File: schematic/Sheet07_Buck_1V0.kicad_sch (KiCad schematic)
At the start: 14 parts, among them U5 TPS7H5001-SP

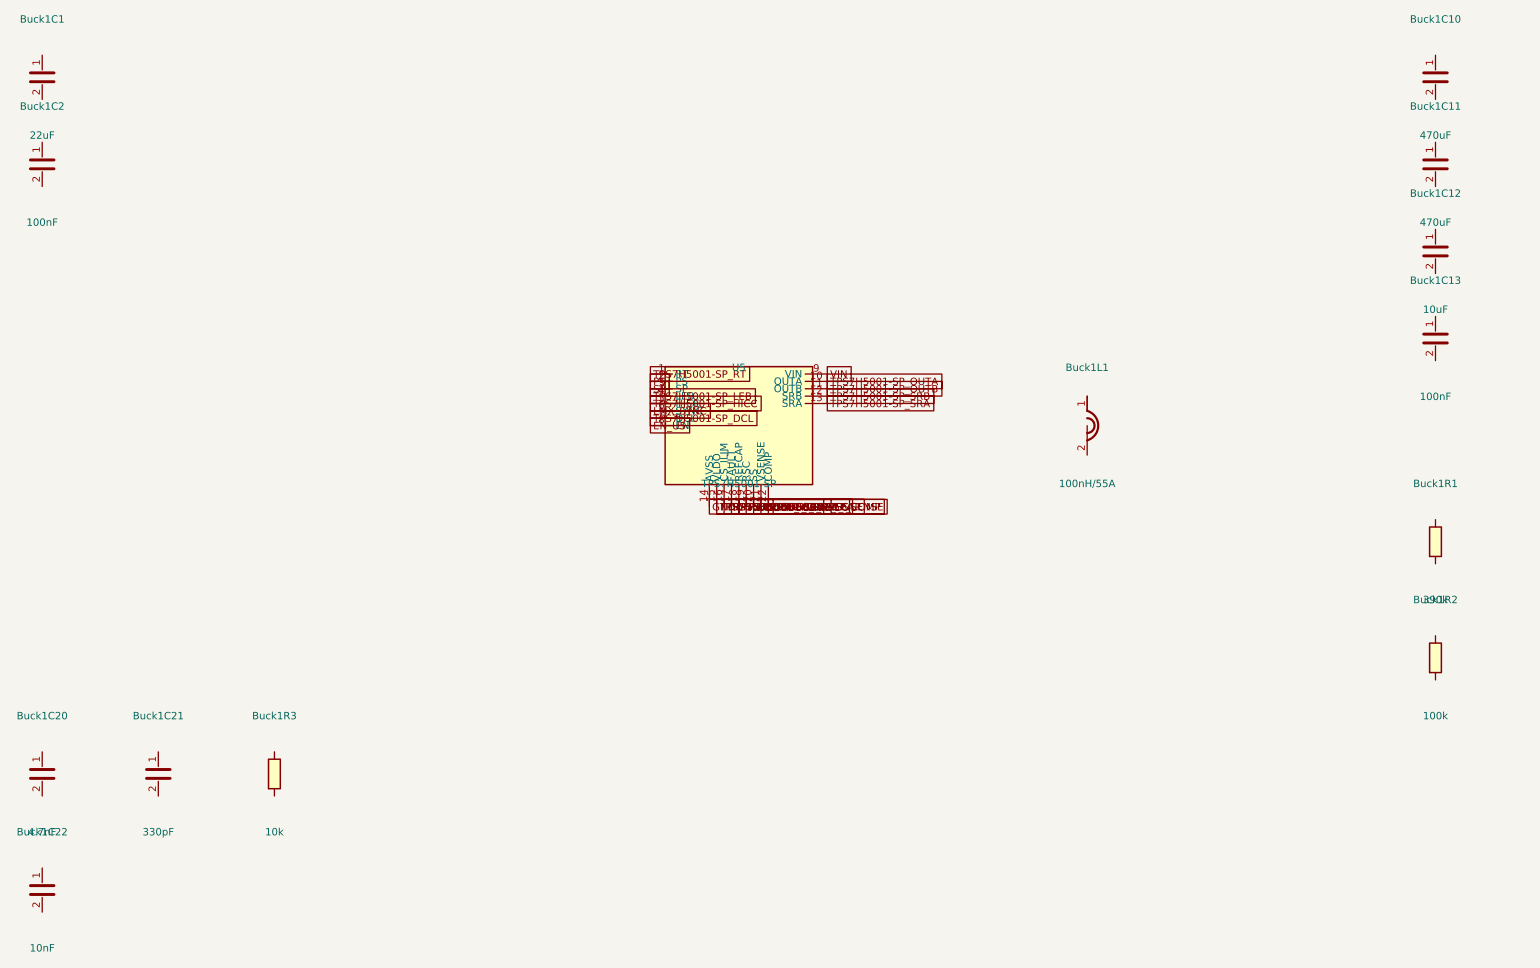
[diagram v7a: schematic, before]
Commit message: feat: connect ALL passive components and fix clock routing
- Added PASSIVE_TOPOLOGY dict mapping 139 passives to their nets
- Passive pin endpoints now get global_labels (was 0 connected, now 138)
- R38 intentionally GND-GND (RECAL_EN pull-down)
- Fixed LMK clock output mapping: CLKout0→ADC_CLK_P, CLKout2→FPGA_REFCLK_P, etc.
- Fixed TPS7H5001-SP SYNC pin collision with LMX_SYNC
- Total connections: 867 pins (up from 641)
- Cross-sheet nets: 52
- Power rails: VIN(33), +3V3(98), GND(228) all with decoupling
- JESD204C: U1↔U2 on 4 lanes ✓
- SPI: U1↔U2↔U3↔U4 ✓
- Clock: LMK→ADC (CLK+SYSREF), LMK→FPGA (REF+SPW) ✓
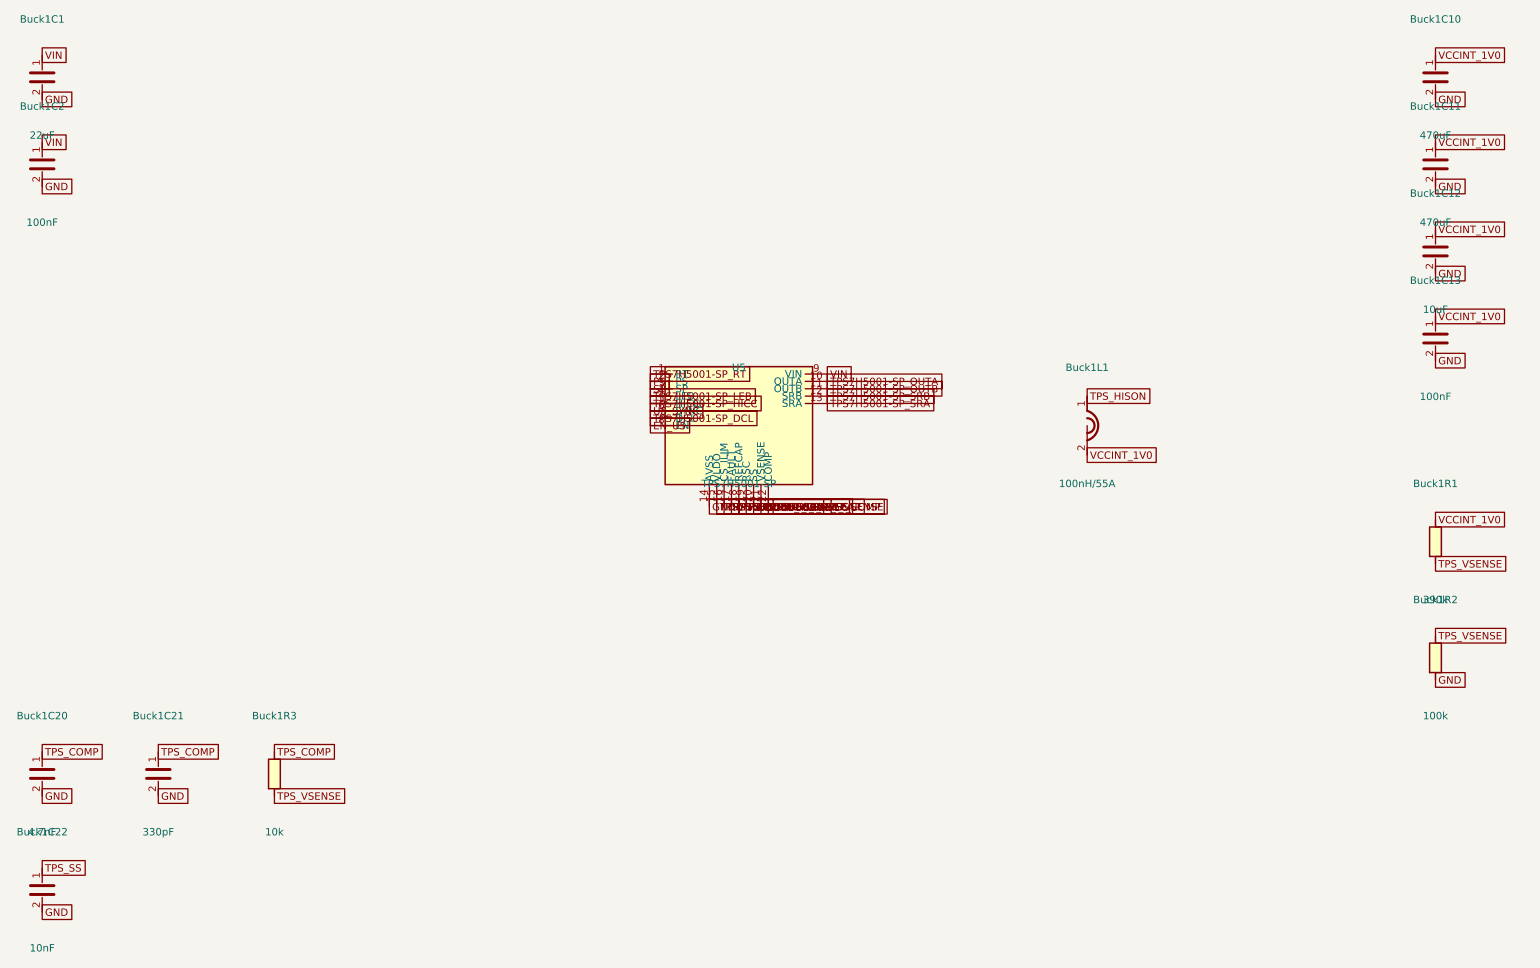
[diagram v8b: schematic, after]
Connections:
- net GND: now also Buck1C1.2, Buck1C10.2, Buck1C11.2, Buck1C12.2, Buck1C13.2, Buck1C2.2, Buck1C20.2, Buck1C21.2, Buck1C22.2, Buck1R2.2
- net VIN: now also Buck1C1.1, Buck1C2.1
- net VCCINT_1V0: now reaches Buck1R1.1
- net VCCINT_1V0: now also Buck1C10.1, Buck1C11.1, Buck1C12.1, Buck1C13.1, Buck1L1.2
- net TPS_VSENSE: now reaches Buck1R1.2
- net TPS_VSENSE: now also Buck1R2.1, Buck1R3.2
- net TPS_HISON: now reaches Buck1L1.1
- net TPS_COMP: now reaches Buck1R3.1
- net TPS_COMP: now also Buck1C20.1, Buck1C21.1
- net TPS_SS: now reaches Buck1C22.1
- net LMX_SYNC renamed U5_SYNC
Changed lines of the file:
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@@
   (global_label "TPS7H5001-SP_LEB" (at 184.7600 94.9200 0) (effects (font (size 1.27 1.27))))
   (global_label "TPS7H5001-SP_HICC" (at 184.7600 96.1900 0) (effects (font (size 1.27 1.27))))
-  (global_label "LMX_SYNC" (at 184.7600 97.4600 0) (effects (font (size 1.27 1.27))))
+  (global_label "U5_SYNC" (at 184.7600 97.4600 0) (effects (font (size 1.27 1.27))))
   (global_label "TPS7H5001-SP_DCL" (at 184.7600 98.7300 0) (effects (font (size 1.27 1.27))))
   (global_label "EN_U5" (at 184.7600 100.0000 0) (effects (font (size 1.27 1.27))))
@@
   (global_label "TPS7H5001-SP_VSENSE" (at 203.8100 113.9700 0) (effects (font (size 1.27 1.27))))
   (global_label "TPS7H5001-SP_COMP" (at 205.0800 113.9700 0) (effects (font (size 1.27 1.27))))
+  (global_label "VIN" (at 80.0000 36.1900 0) (effects (font (size 1.27 1.27))))
+  (global_label "GND" (at 80.0000 43.8100 0) (effects (font (size 1.27 1.27))))
+  (global_label "VIN" (at 80.0000 51.1900 0) (effects (font (size 1.27 1.27))))
+  (global_label "GND" (at 80.0000 58.8100 0) (effects (font (size 1.27 1.27))))
+  (global_label "VCCINT_1V0" (at 320.0000 36.1900 0) (effects (font (size 1.27 1.27))))
+  (global_label "GND" (at 320.0000 43.8100 0) (effects (font (size 1.27 1.27))))
+  (global_label "VCCINT_1V0" (at 320.0000 51.1900 0) (effects (font (size 1.27 1.27))))
+  (global_label "GND" (at 320.0000 58.8100 0) (effects (font (size 1.27 1.27))))
+  (global_label "VCCINT_1V0" (at 320.0000 66.1900 0) (effects (font (size 1.27 1.27))))
+  (global_label "GND" (at 320.0000 73.8100 0) (effects (font (size 1.27 1.27))))
+  (global_label "VCCINT_1V0" (at 320.0000 81.1900 0) (effects (font (size 1.27 1.27))))
+  (global_label "GND" (at 320.0000 88.8100 0) (effects (font (size 1.27 1.27))))
+  (global_label "TPS_HISON" (at 260.0000 94.9200 0) (effects (font (size 1.27 1.27))))
+  (global_label "VCCINT_1V0" (at 260.0000 105.0800 0) (effects (font (size 1.27 1.27))))
+  (global_label "VCCINT_1V0" (at 320.0000 116.1900 0) (effects (font (size 1.27 1.27))))
+  (global_label "TPS_VSENSE" (at 320.0000 123.8100 0) (effects (font (size 1.27 1.27))))
+  (global_label "TPS_VSENSE" (at 320.0000 136.1900 0) (effects (font (size 1.27 1.27))))
+  (global_label "GND" (at 320.0000 143.8100 0) (effects (font (size 1.27 1.27))))
+  (global_label "TPS_COMP" (at 80.0000 156.1900 0) (effects (font (size 1.27 1.27))))
+  (global_label "GND" (at 80.0000 163.8100 0) (effects (font (size 1.27 1.27))))
+  (global_label "TPS_COMP" (at 100.0000 156.1900 0) (effects (font (size 1.27 1.27))))
+  (global_label "GND" (at 100.0000 163.8100 0) (effects (font (size 1.27 1.27))))
+  (global_label "TPS_COMP" (at 120.0000 156.1900 0) (effects (font (size 1.27 1.27))))
+  (global_label "TPS_VSENSE" (at 120.0000 163.8100 0) (effects (font (size 1.27 1.27))))
+  (global_label "TPS_SS" (at 80.0000 176.1900 0) (effects (font (size 1.27 1.27))))
+  (global_label "GND" (at 80.0000 183.8100 0) (effects (font (size 1.27 1.27))))
   (sheet_instances (path "/" (page "1")))
 )
